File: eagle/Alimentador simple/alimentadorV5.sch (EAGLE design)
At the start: 32 parts, among them T1 AO3403, T2 AO3403, T3 AO3403, T4 AO3403, T5 AO3403

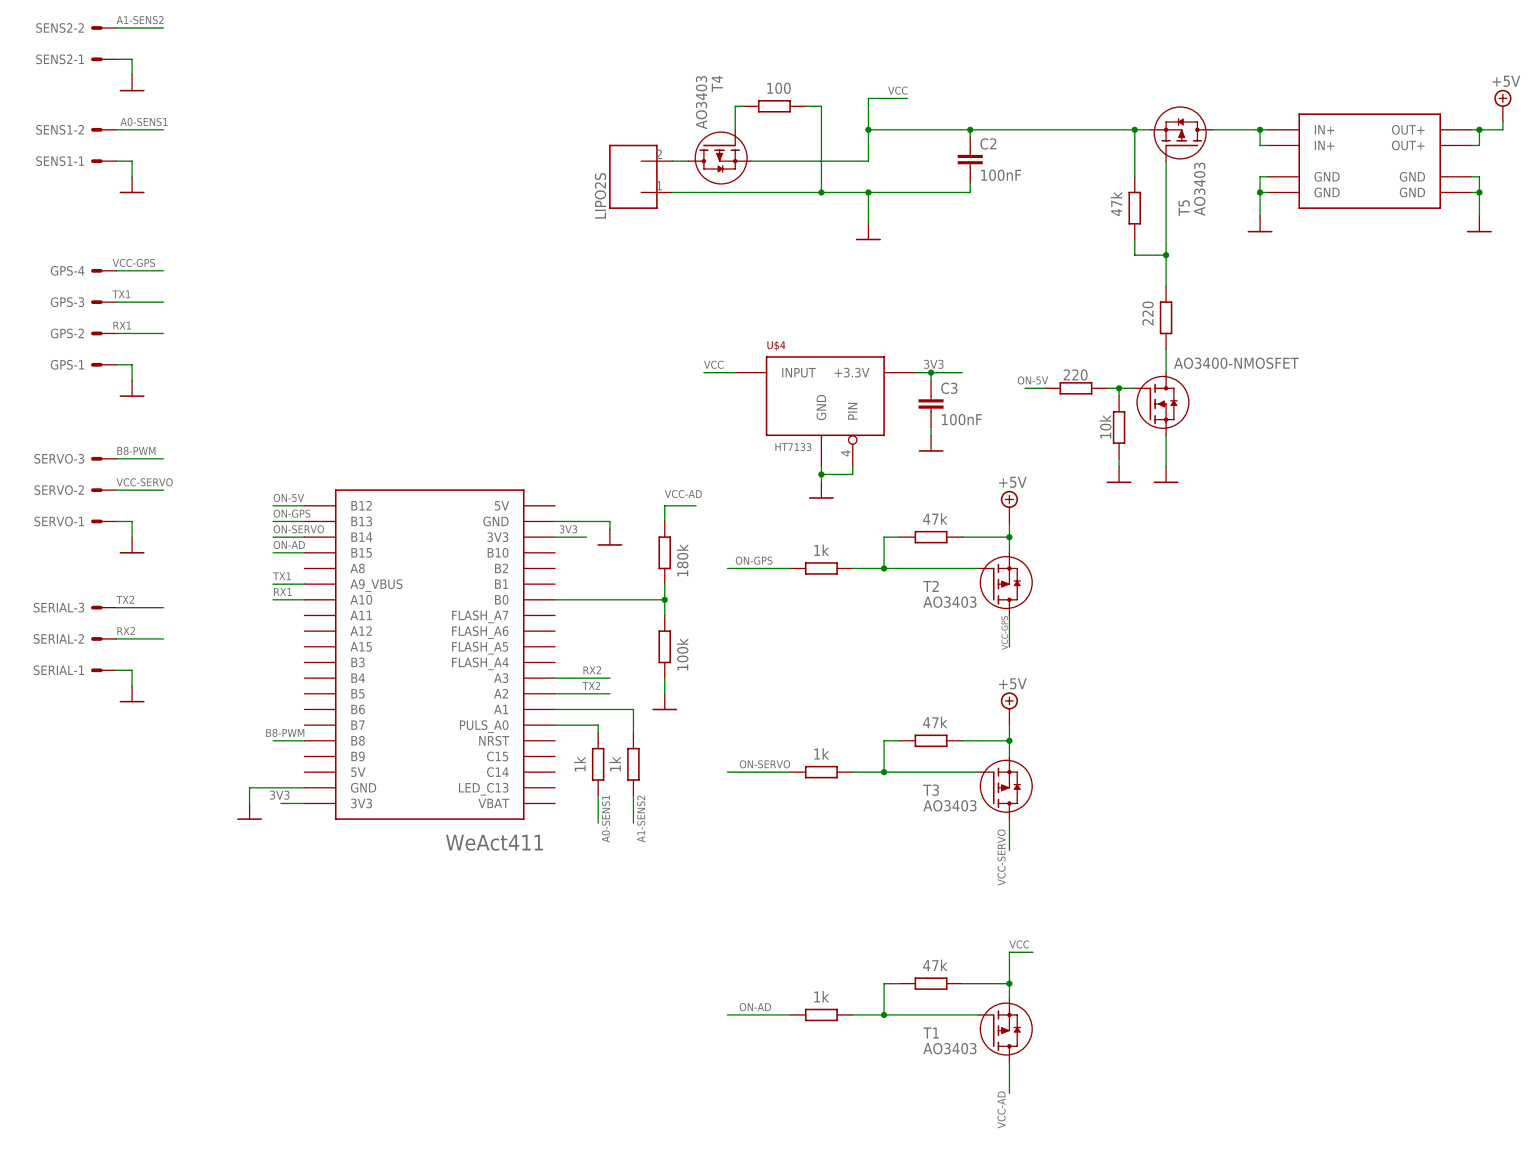
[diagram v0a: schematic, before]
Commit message: Con posiciones de servo
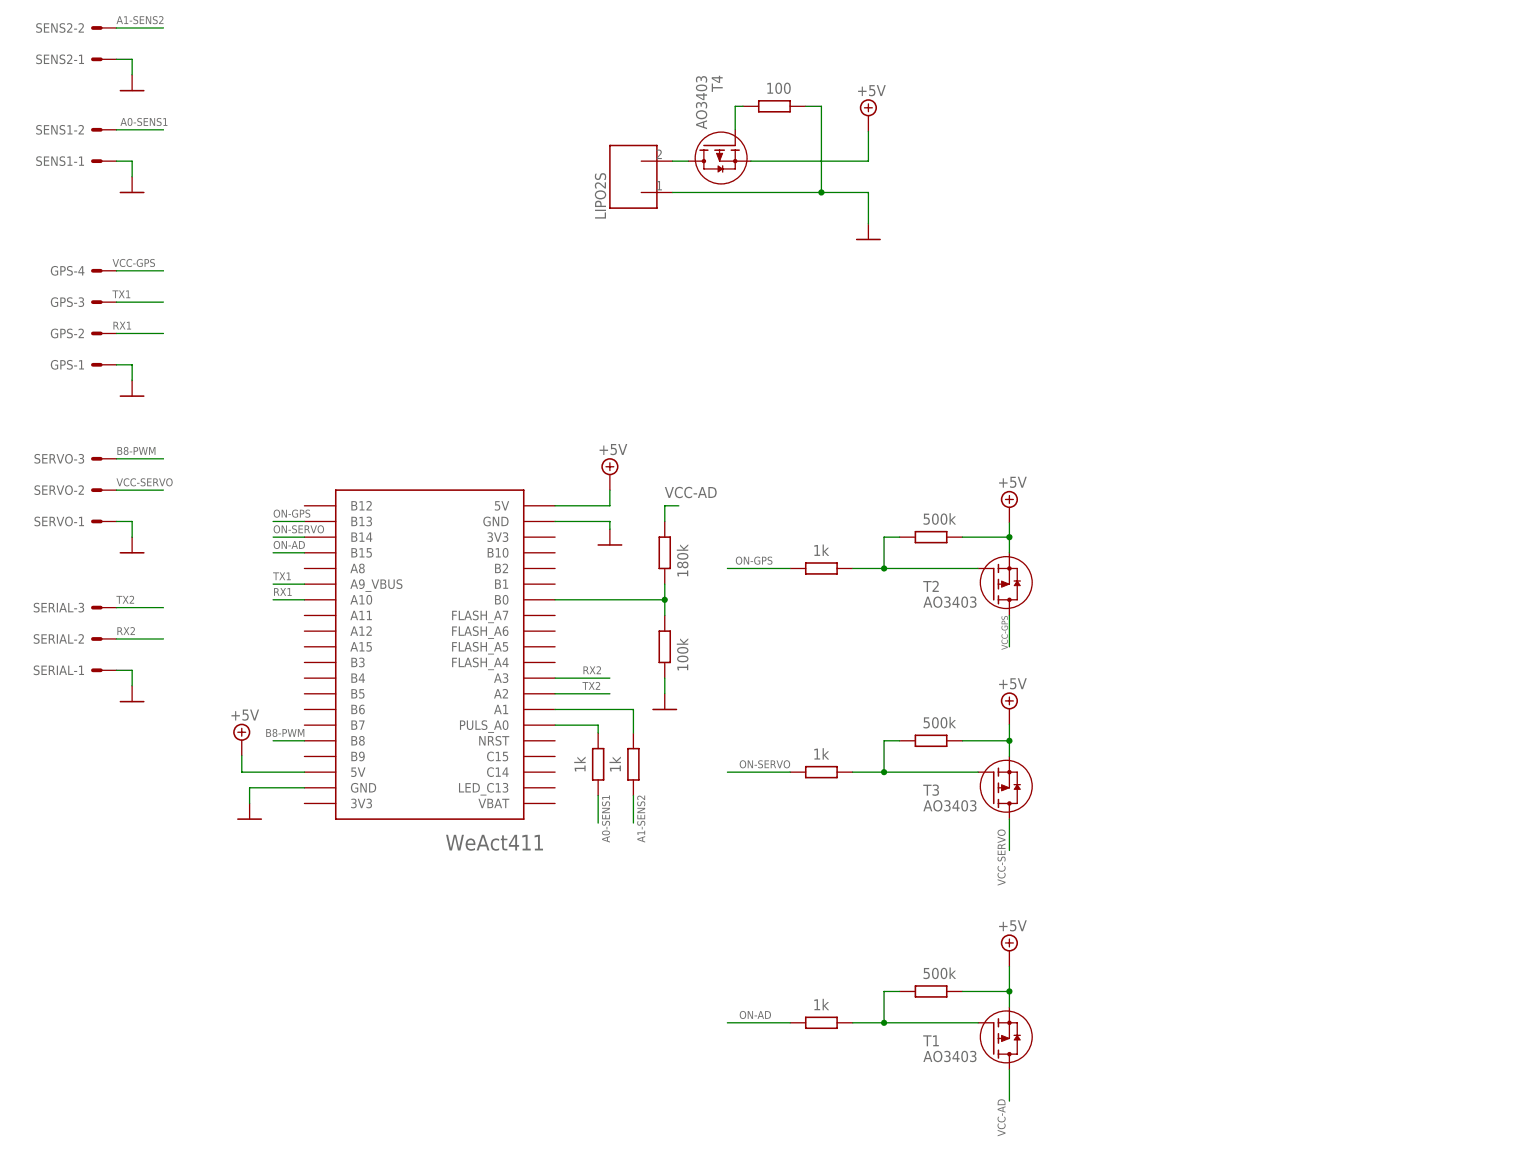
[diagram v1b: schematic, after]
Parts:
- removed C2, C3: 100nF, rcl:C-EUC1206
- removed R10, R9: 220, rcl:R-EU_R1206
- removed R15: 10k, rcl:R-EU_R1206
- removed R8: 47k, rcl:R-EU_R1206
- removed T5: AO3403, jcf:AO3403
- removed U$1: AO3400-NMOSFET, jcf:AO3400-NMOSFET
- removed U$3: REG12TO5, jcf:REG12TO5
- removed U$4: HT7133, jcf:HT7133
- R1, R11, R5: value 47k -> 500k
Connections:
- removed net 3V3: C3.1, U$2.3V3@1, U$2.3V3@2, U$4.+3.3V
- removed net KK: T5.D, U$3.IN+@1, U$3.IN+@2
- removed net N$4: R8.1, R9.2, T5.G
- removed net N$7: R10.1, R15.1, U$1.G
- removed net ON-5V: R10.2, U$2.B12
- removed net UU: R9.1, U$1.D
- removed net VCC: C2.1, R11.2, R8.2, T1.S, T4.S, T5.S, U$4.INPUT
- net +5V: now also R11.2, T1.S, T4.S, U$2.5V@1, U$2.5V@2; no longer U$3.OUT+@1, U$3.OUT+@2
- net GND: no longer C2.2, C3.2, R15.2, U$1.S, U$3.GND@1, U$3.GND@2, U$3.GND@3, U$3.GND@4, U$4.GND, U$4.PIN
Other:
- moved on the sheet: T1
